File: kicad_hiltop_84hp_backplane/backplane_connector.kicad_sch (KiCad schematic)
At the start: 40 parts, among them J1 CONN_DIN_HDR_96POS, J2 CONN_DIN_HDR_96POS, J3 CONN_DIN_HDR_96POS, J4 CONN_DIN_HDR_96POS, J5 CONN_DIN_HDR_96POS, J6 CONN_DIN_HDR_96POS, U3 LTC4311, U4 LTC4311

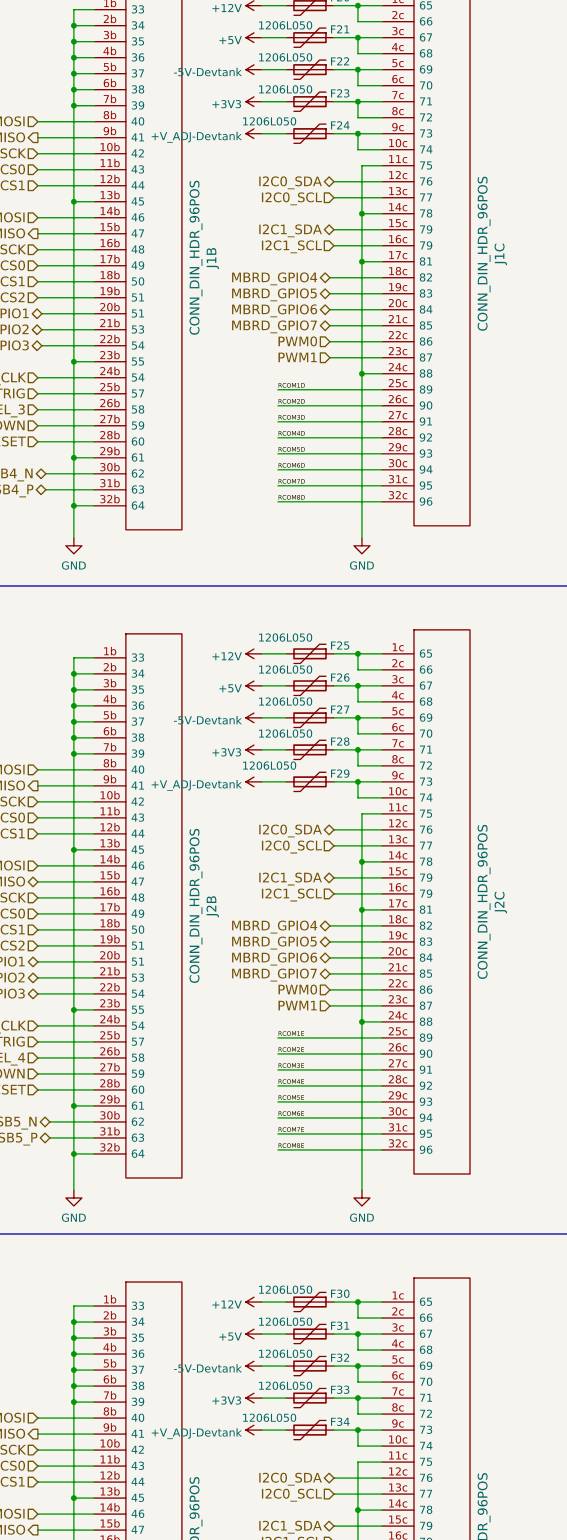
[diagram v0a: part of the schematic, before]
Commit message: Updated layout with throwdown, added slots and resized board
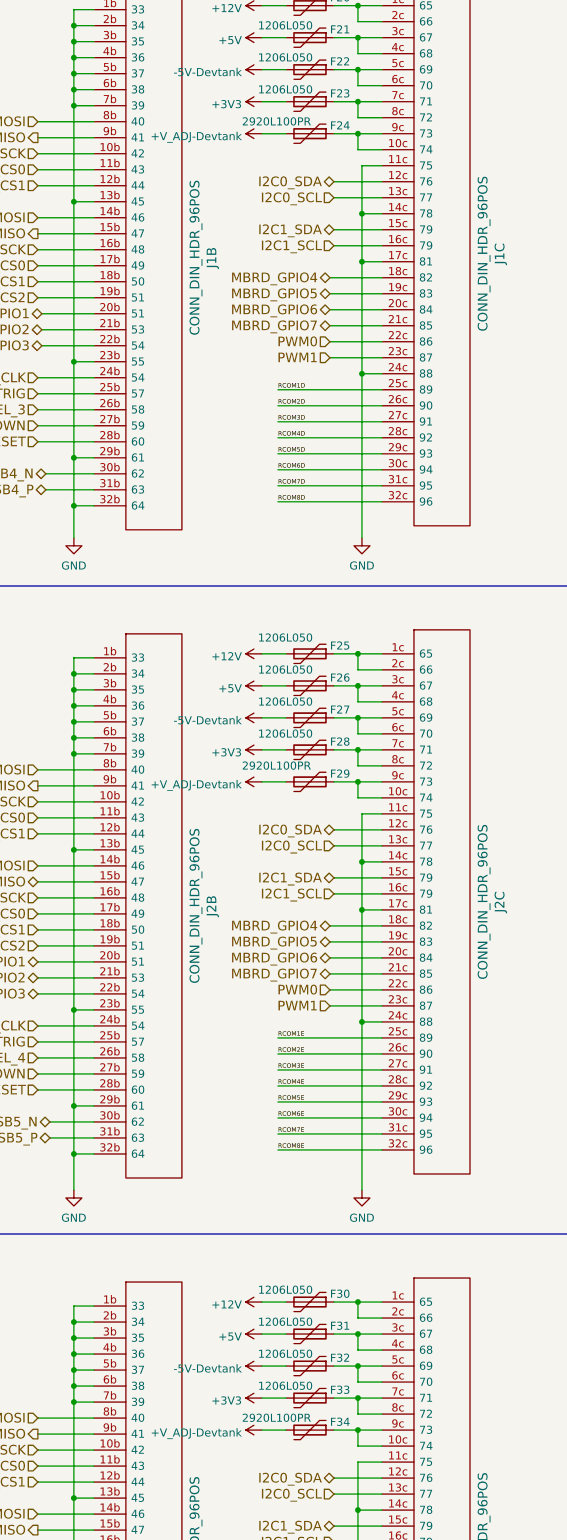
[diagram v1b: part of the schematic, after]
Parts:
- F24, F29, F34: value 1206L050 -> 2920L100PR; footprint Fuse:Fuse_1206_3216Metric -> Fuse:Fuse_2920_7451Metric
- J1, J2, J3, J4, J5, J6: footprint Connectors_IEC_DIN:Socket_DIN41612-CaseC1-full-Female-96Pin-3rows -> Devtank_PCB_Lib:Socket_DIN41612-CaseC1-full-Female-96Pin-3rows
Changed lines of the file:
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@@
       (effects (font (size 1.524 1.524)))
     )
-    (property "Footprint" "Connectors_IEC_DIN:Socket_DIN41612-CaseC1-full-Female-96Pin-3rows" (id 2) (at 120.015 27.94 0)
+    (property "Footprint" "Devtank_PCB_Lib:Socket_DIN41612-CaseC1-full-Female-96Pin-3rows" (id 2) (at 120.015 27.94 0)
       (effects (font (size 1.524 1.524)) hide)
     )
@@
       (effects (font (size 1.524 1.524)))
     )
-    (property "Footprint" "Connectors_IEC_DIN:Socket_DIN41612-CaseC1-full-Female-96Pin-3rows" (id 2) (at 120.015 130.81 0)
+    (property "Footprint" "Devtank_PCB_Lib:Socket_DIN41612-CaseC1-full-Female-96Pin-3rows" (id 2) (at 120.015 130.81 0)
       (effects (font (size 1.524 1.524)) hide)
     )
@@
       (effects (font (size 1.524 1.524)))
     )
-    (property "Footprint" "Connectors_IEC_DIN:Socket_DIN41612-CaseC1-full-Female-96Pin-3rows" (id 2) (at 120.015 233.68 0)
+    (property "Footprint" "Devtank_PCB_Lib:Socket_DIN41612-CaseC1-full-Female-96Pin-3rows" (id 2) (at 120.015 233.68 0)
       (effects (font (size 1.524 1.524)) hide)
     )
@@
       (effects (font (size 1.524 1.524)))
     )
-    (property "Footprint" "Connectors_IEC_DIN:Socket_DIN41612-CaseC1-full-Female-96Pin-3rows" (id 2) (at 167.005 27.94 0)
+    (property "Footprint" "Devtank_PCB_Lib:Socket_DIN41612-CaseC1-full-Female-96Pin-3rows" (id 2) (at 167.005 27.94 0)
       (effects (font (size 1.524 1.524)) hide)
     )
@@
       (effects (font (size 1.524 1.524)))
     )
-    (property "Footprint" "Connectors_IEC_DIN:Socket_DIN41612-CaseC1-full-Female-96Pin-3rows" (id 2) (at 167.005 130.81 0)
+    (property "Footprint" "Devtank_PCB_Lib:Socket_DIN41612-CaseC1-full-Female-96Pin-3rows" (id 2) (at 167.005 130.81 0)
       (effects (font (size 1.524 1.524)) hide)
     )
@@
       (effects (font (size 1.524 1.524)))
     )
-    (property "Footprint" "Connectors_IEC_DIN:Socket_DIN41612-CaseC1-full-Female-96Pin-3rows" (id 2) (at 167.005 233.68 0)
+    (property "Footprint" "Devtank_PCB_Lib:Socket_DIN41612-CaseC1-full-Female-96Pin-3rows" (id 2) (at 167.005 233.68 0)
       (effects (font (size 1.524 1.524)) hide)
     )
@@
       (effects (font (size 1.524 1.524)))
     )
-    (property "Footprint" "Connectors_IEC_DIN:Socket_DIN41612-CaseC1-full-Female-96Pin-3rows" (id 2) (at 212.725 27.305 0)
+    (property "Footprint" "Devtank_PCB_Lib:Socket_DIN41612-CaseC1-full-Female-96Pin-3rows" (id 2) (at 212.725 27.305 0)
       (effects (font (size 1.524 1.524)) hide)
     )
@@
       (effects (font (size 1.524 1.524)))
     )
-    (property "Footprint" "Connectors_IEC_DIN:Socket_DIN41612-CaseC1-full-Female-96Pin-3rows" (id 2) (at 212.725 130.175 0)
+    (property "Footprint" "Devtank_PCB_Lib:Socket_DIN41612-CaseC1-full-Female-96Pin-3rows" (id 2) (at 212.725 130.175 0)
       (effects (font (size 1.524 1.524)) hide)
     )
@@
       (effects (font (size 1.524 1.524)))
     )
-    (property "Footprint" "Connectors_IEC_DIN:Socket_DIN41612-CaseC1-full-Female-96Pin-3rows" (id 2) (at 212.725 233.045 0)
+    (property "Footprint" "Devtank_PCB_Lib:Socket_DIN41612-CaseC1-full-Female-96Pin-3rows" (id 2) (at 212.725 233.045 0)
       (effects (font (size 1.524 1.524)) hide)
     )
@@
       (effects (font (size 1.27 1.27)) (justify left))
     )
-    (property "Value" "1206L050" (id 1) (at 426.72 150.495 90)
+    (property "Value" "2920L100PR" (id 1) (at 426.72 150.495 90)
       (effects (font (size 1.27 1.27)) (justify left))
     )
-    (property "Footprint" "Fuse:Fuse_1206_3216Metric" (id 2) (at 432.435 154.305 0)
+    (property "Footprint" "Fuse:Fuse_2920_7451Metric" (id 2) (at 432.435 154.305 0)
       (effects (font (size 1.27 1.27)) (justify left) hide)
     )
@@
       (effects (font (size 1.27 1.27)) (justify left))
     )
-    (property "Value" "1206L050" (id 1) (at 426.72 48.26 90)
+    (property "Value" "2920L100PR" (id 1) (at 426.72 48.26 90)
       (effects (font (size 1.27 1.27)) (justify left))
     )
-    (property "Footprint" "Fuse:Fuse_1206_3216Metric" (id 2) (at 432.435 51.435 0)
+    (property "Footprint" "Fuse:Fuse_2920_7451Metric" (id 2) (at 432.435 51.435 0)
       (effects (font (size 1.27 1.27)) (justify left) hide)
     )
@@
       (effects (font (size 1.524 1.524)))
     )
-    (property "Footprint" "Connectors_IEC_DIN:Socket_DIN41612-CaseC1-full-Female-96Pin-3rows" (id 2) (at 457.835 130.175 0)
+    (property "Footprint" "Devtank_PCB_Lib:Socket_DIN41612-CaseC1-full-Female-96Pin-3rows" (id 2) (at 457.835 130.175 0)
       (effects (font (size 1.524 1.524)) hide)
     )
@@
       (effects (font (size 1.524 1.524)))
     )
-    (property "Footprint" "Connectors_IEC_DIN:Socket_DIN41612-CaseC1-full-Female-96Pin-3rows" (id 2) (at 412.115 233.68 0)
+    (property "Footprint" "Devtank_PCB_Lib:Socket_DIN41612-CaseC1-full-Female-96Pin-3rows" (id 2) (at 412.115 233.68 0)
       (effects (font (size 1.524 1.524)) hide)
     )
@@
       (effects (font (size 1.524 1.524)))
     )
-    (property "Footprint" "Connectors_IEC_DIN:Socket_DIN41612-CaseC1-full-Female-96Pin-3rows" (id 2) (at 457.835 27.305 0)
+    (property "Footprint" "Devtank_PCB_Lib:Socket_DIN41612-CaseC1-full-Female-96Pin-3rows" (id 2) (at 457.835 27.305 0)
       (effects (font (size 1.524 1.524)) hide)
     )
@@
       (effects (font (size 1.524 1.524)))
     )
-    (property "Footprint" "Connectors_IEC_DIN:Socket_DIN41612-CaseC1-full-Female-96Pin-3rows" (id 2) (at 365.125 27.94 0)
+    (property "Footprint" "Devtank_PCB_Lib:Socket_DIN41612-CaseC1-full-Female-96Pin-3rows" (id 2) (at 365.125 27.94 0)
       (effects (font (size 1.524 1.524)) hide)
     )
@@
       (effects (font (size 1.524 1.524)))
     )
-    (property "Footprint" "Connectors_IEC_DIN:Socket_DIN41612-CaseC1-full-Female-96Pin-3rows" (id 2) (at 412.115 27.94 0)
+    (property "Footprint" "Devtank_PCB_Lib:Socket_DIN41612-CaseC1-full-Female-96Pin-3rows" (id 2) (at 412.115 27.94 0)
       (effects (font (size 1.524 1.524)) hide)
     )
@@
       (effects (font (size 1.524 1.524)))
     )
-    (property "Footprint" "Connectors_IEC_DIN:Socket_DIN41612-CaseC1-full-Female-96Pin-3rows" (id 2) (at 365.125 233.68 0)
+    (property "Footprint" "Devtank_PCB_Lib:Socket_DIN41612-CaseC1-full-Female-96Pin-3rows" (id 2) (at 365.125 233.68 0)
       (effects (font (size 1.524 1.524)) hide)
     )
@@
       (effects (font (size 1.524 1.524)))
     )
-    (property "Footprint" "Connectors_IEC_DIN:Socket_DIN41612-CaseC1-full-Female-96Pin-3rows" (id 2) (at 365.125 130.81 0)
+    (property "Footprint" "Devtank_PCB_Lib:Socket_DIN41612-CaseC1-full-Female-96Pin-3rows" (id 2) (at 365.125 130.81 0)
       (effects (font (size 1.524 1.524)) hide)
     )
@@
       (effects (font (size 1.524 1.524)))
     )
-    (property "Footprint" "Connectors_IEC_DIN:Socket_DIN41612-CaseC1-full-Female-96Pin-3rows" (id 2) (at 457.835 233.045 0)
+    (property "Footprint" "Devtank_PCB_Lib:Socket_DIN41612-CaseC1-full-Female-96Pin-3rows" (id 2) (at 457.835 233.045 0)
       (effects (font (size 1.524 1.524)) hide)
     )
@@
       (effects (font (size 1.524 1.524)))
     )
-    (property "Footprint" "Connectors_IEC_DIN:Socket_DIN41612-CaseC1-full-Female-96Pin-3rows" (id 2) (at 412.115 130.81 0)
+    (property "Footprint" "Devtank_PCB_Lib:Socket_DIN41612-CaseC1-full-Female-96Pin-3rows" (id 2) (at 412.115 130.81 0)
       (effects (font (size 1.524 1.524)) hide)
     )
@@
       (effects (font (size 1.27 1.27)) (justify left))
     )
-    (property "Value" "1206L050" (id 1) (at 426.72 254 90)
+    (property "Value" "2920L100PR" (id 1) (at 426.72 254 90)
       (effects (font (size 1.27 1.27)) (justify left))
     )
-    (property "Footprint" "Fuse:Fuse_1206_3216Metric" (id 2) (at 432.435 257.175 0)
+    (property "Footprint" "Fuse:Fuse_2920_7451Metric" (id 2) (at 432.435 257.175 0)
       (effects (font (size 1.27 1.27)) (justify left) hide)
     )

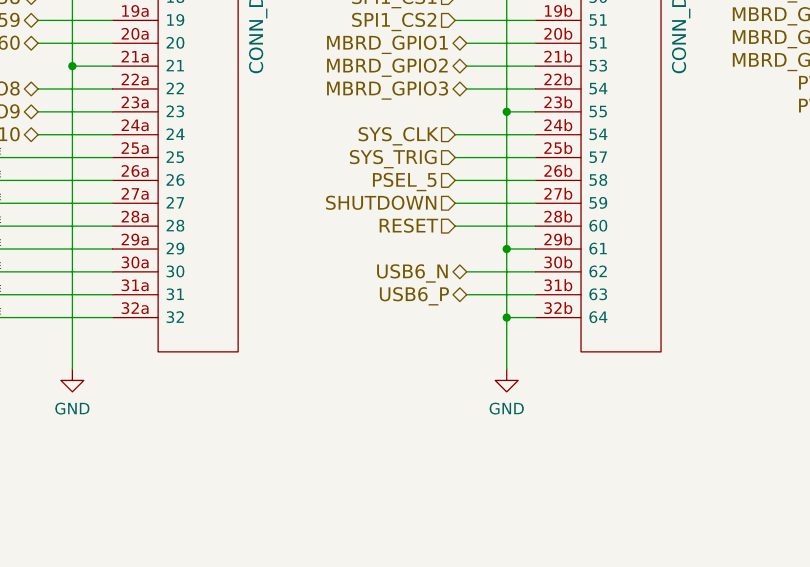
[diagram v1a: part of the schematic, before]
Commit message: Started differential tracking on layout
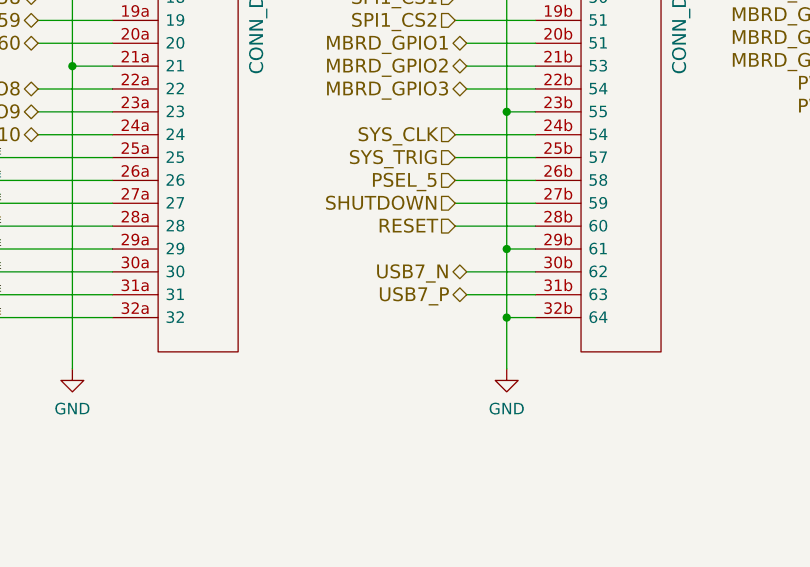
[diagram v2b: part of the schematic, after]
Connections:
- net USB6_N renamed USB7_N
- net USB6_P renamed USB7_P
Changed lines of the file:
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@@
     (effects (font (size 1.524 1.524)) (justify right))
   )
-  (hierarchical_label "USB6_N" (shape bidirectional) (at 395.605 309.88 180)
+  (hierarchical_label "USB7_N" (shape bidirectional) (at 395.605 309.88 180)
     (effects (font (size 1.524 1.524)) (justify right))
   )
@@
     (effects (font (size 1.524 1.524)) (justify right))
   )
-  (hierarchical_label "USB6_P" (shape bidirectional) (at 395.605 312.42 180)
-    (effects (font (size 1.524 1.524)) (justify right))
-  )
+  (hierarchical_label "USB7_P" (shape bidirectional) (at 395.605 312.42 180)
+    (effects (font (size 1.524 1.524)) (justify right))
+  )

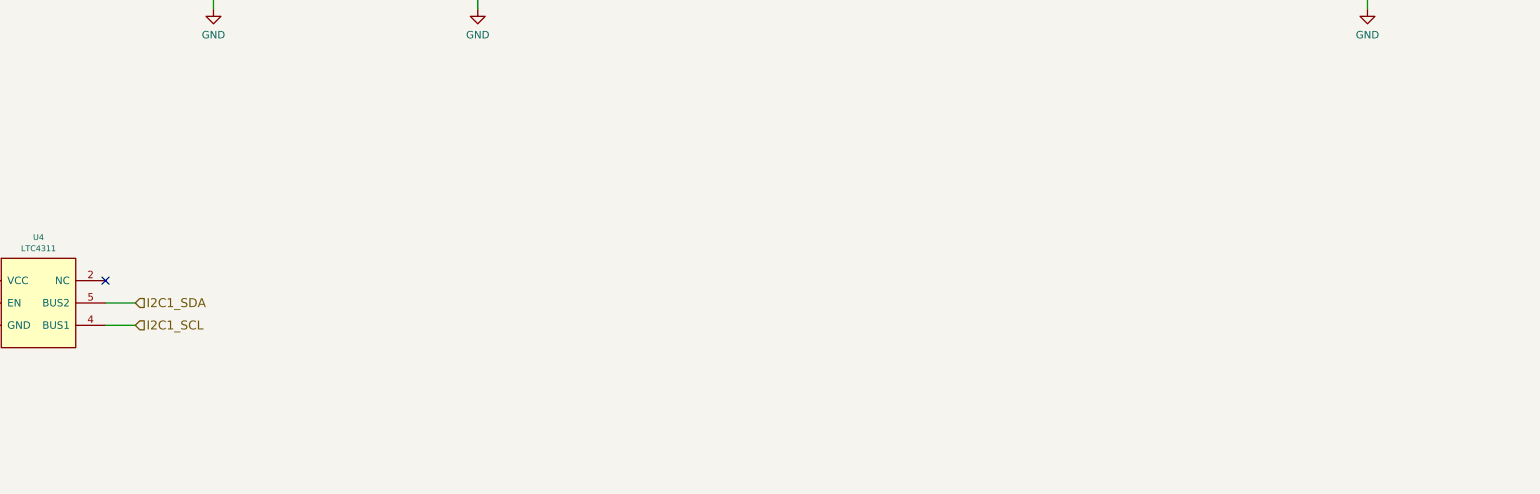
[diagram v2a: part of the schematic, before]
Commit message: Added io tracking on the layout
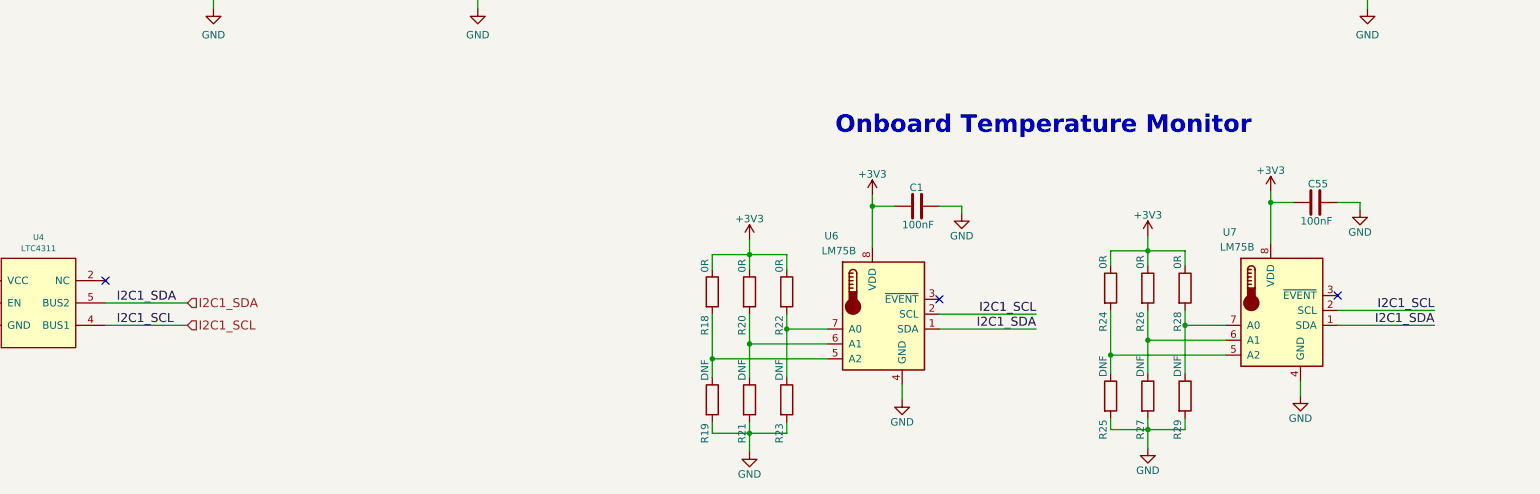
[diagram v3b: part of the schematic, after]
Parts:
- added C1, C55: 100nF, Capacitor_SMD:C_0402_1005Metric, symbol Device:C
- added R18, R20, R22, R24, R26, R28: 0R, Resistor_SMD:R_0402_1005Metric, symbol Device:R
- added R19, R21, R23, R25, R27, R29: DNF, Resistor_SMD:R_0402_1005Metric, symbol Device:R
- added U6, U7: LM75B, Package_SO:SOIC-8_3.9x4.9mm_P1.27mm, symbol HILTOP_Motherboard-rescue:AT30TS75-Devtank
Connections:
- net +3V3: now also C1.2, C55.2, R18.1, R20.1, R22.1, R24.1, R26.1, R28.1, U6.8 (VDD), U7.8 (VDD)
- net GND: now also C1.1, C55.1, R19.2, R21.2, R23.2, R25.2, R27.2, R29.2, U6.4 (GND), U7.4 (GND)
- net I2C1_SCL: now also U6.2 (SCL), U7.2 (SCL)
- net I2C1_SDA: now also U6.1 (SDA), U7.1 (SDA)
- new net: R18.2, R19.1, U6.5 (A2)
- new net: R28.2, R29.1, U7.7 (A0)
- new net: R24.2, R25.1, U7.5 (A2)
- new net: R26.2, R27.1, U7.6 (A1)
- new net: R20.2, R21.1, U6.6 (A1)
- new net: R22.2, R23.1, U6.7 (A0)
- no-connect marks 18 -> 20
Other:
- note added: "Onboard Temperature Monitor"
